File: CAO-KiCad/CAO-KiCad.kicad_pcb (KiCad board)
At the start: 2 copper layers, 68.6 x 53.3 mm, 8 parts, among them P1 Power, P2 Analog, P3 Digital, P4 Digital, P5 CONN_01X01, P6 CONN_01X01, P7 CONN_01X01, P8 CONN_01X01

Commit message: Debut de la creation du module ESP32
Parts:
- added D1: LED, LED_SMD:LED_0805_2012Metric_Pad1.15x1.40mm_HandSolder, F.Cu at (140.2, 85.7)
- added J1: Conn_01x03, Connector_PinHeader_2.54mm:PinHeader_1x03_P2.54mm_Vertical, F.Cu at (184.7, 75.6)
- added R1: 470, Resistor_SMD:R_0805_2012Metric_Pad1.20x1.40mm_HandSolder, F.Cu at (144.0, 85.7)
- added U1: MODULE-38P-ESP32-WROOM-32D, RF_Module:ESP32-WROOM-32, F.Cu at (164.2, 103.5)
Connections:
- net /10(**/SS) renamed /10(**/SS)
- net /11(**/MOSI) renamed /11(**/MOSI)
- P1 pad 1: Net-(P1-Pad1) -> unconnected-(P1-Pad1)
- P5 pad 1: Net-(P5-Pad1) -> unconnected-(P5-Pad1)
- P6 pad 1: Net-(P6-Pad1) -> unconnected-(P6-Pad1)
- P7 pad 1: Net-(P7-Pad1) -> unconnected-(P7-Pad1)
- P8 pad 1: Net-(P8-Pad1) -> unconnected-(P8-Pad1)
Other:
- board outline removed
- copper layers 2 -> 4
- board text added: "${COMPAGNY}"
- board text added: "${REVNUM}"

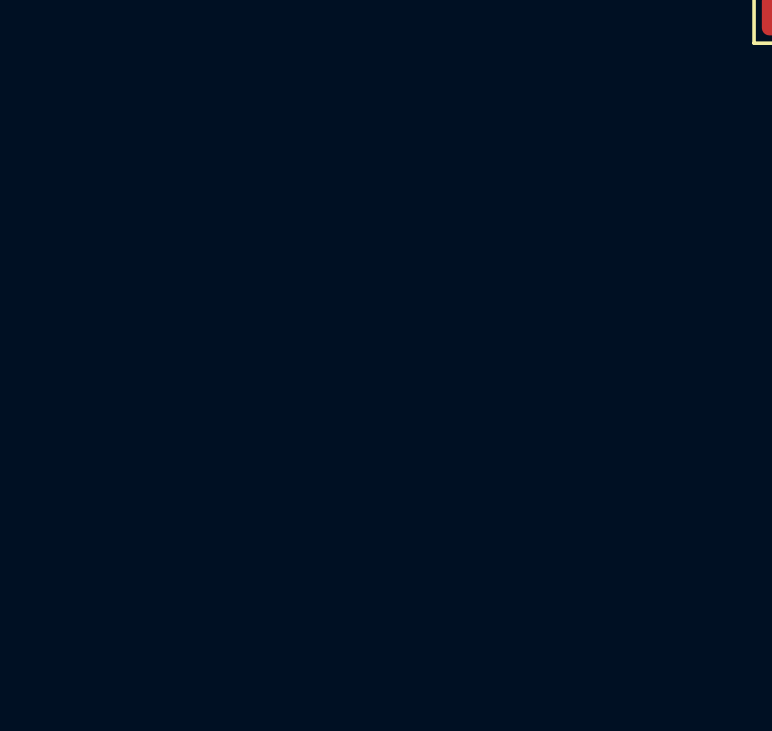
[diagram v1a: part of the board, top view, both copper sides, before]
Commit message: Arrangement des broches du symbole de l'ESP32
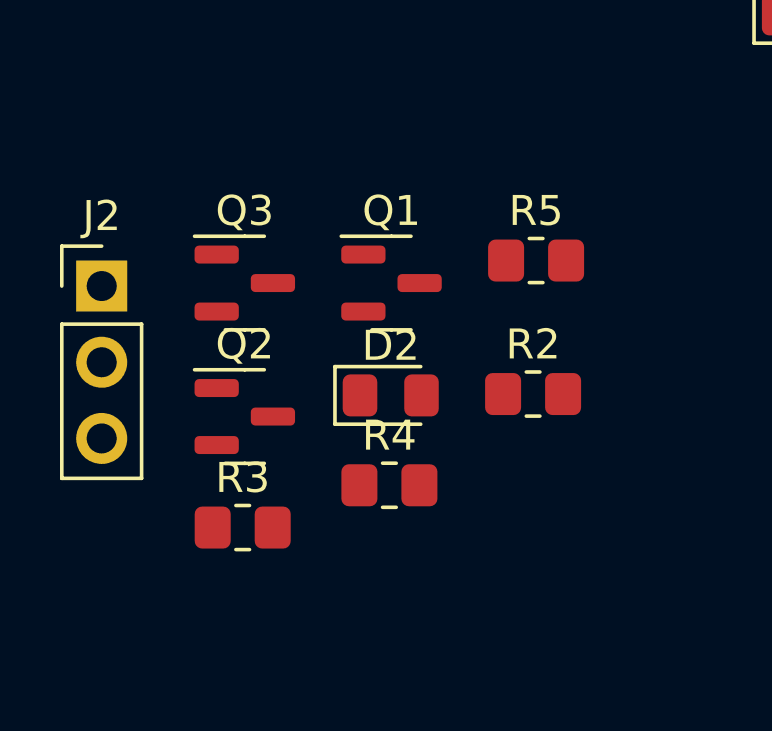
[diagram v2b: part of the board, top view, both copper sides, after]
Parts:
- added D2: LED, LED_SMD:LED_0805_2012Metric_Pad1.15x1.40mm_HandSolder, F.Cu at (126.2, 98.4)
- added J2: OUT1, Connector_PinHeader_2.54mm:PinHeader_1x03_P2.54mm_Vertical, F.Cu at (116.6, 94.8)
- added Q1: AO3402, Package_TO_SOT_SMD:SOT-23, F.Cu at (126.3, 94.7)
- added Q2: IRLML6402, Package_TO_SOT_SMD:SOT-23, F.Cu at (121.4, 99.1)
- added Q3: AO3402, Package_TO_SOT_SMD:SOT-23, F.Cu at (121.4, 94.7)
- added R2: R, Resistor_SMD:R_0805_2012Metric_Pad1.20x1.40mm_HandSolder, F.Cu at (131.0, 98.4)
- added R3: 560, Resistor_SMD:R_0805_2012Metric_Pad1.20x1.40mm_HandSolder, F.Cu at (121.3, 102.8)
- added R4: 10k, Resistor_SMD:R_0805_2012Metric_Pad1.20x1.40mm_HandSolder, F.Cu at (126.2, 101.4)
- added R5: 10k, Resistor_SMD:R_0805_2012Metric_Pad1.20x1.40mm_HandSolder, F.Cu at (131.1, 93.9)
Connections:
- U1 pad 1: unconnected-(U1-Pad1) -> +3V3
- U1 pad 15: (no net) -> unconnected-(U1-Pad15)
- U1 pad 18: +5V -> unconnected-(U1-Pad18)
- U1 pad 19: unconnected-(U1-Pad19) -> +5V
- U1 pad 2: (no net) -> unconnected-(U1-Pad2)
- U1 pad 32: (no net) -> unconnected-(U1-Pad32)
- U1 pad 38: unconnected-(U1-Pad38) -> GND

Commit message: MAJ empreinte
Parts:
- added S1: Gaz_Sensor, Package_TO_SOT_THT:TO-5-2_Window, F.Cu at (125.1, 84.3)
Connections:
- U1 pad 4: unconnected-(U1-Pad4) -> Net-(U1-Pad4)
- U1 pad 9: unconnected-(U1-Pad9) -> Net-(S1-Pad4)
